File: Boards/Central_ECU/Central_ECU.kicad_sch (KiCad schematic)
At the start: 88 parts, among them J1 Micro_SD_Card, U1 SSD1306, U2 STM32G0B1RCTx, U3 TCAN1046, U9 LPS22HH, Y1 8MHz, Y2 32.768k

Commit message: Updates to board to refelct rework state
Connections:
- net CAN1_RX: now also TP10.1, TP11.1, TP8.1, U2.25 (PC4), U2.26 (PC5), U3.4 (RXD1), U3.6 (TXD2), U3.7 (RXD2); no longer U2.27 (PB0)
- net CAN2_RX: now also U2.27 (PB0); no longer TP10.1, U2.25 (PC4), U3.6 (TXD2)
- net CAN2_TX: now also U2.28 (PB1); no longer TP11.1, U2.26 (PC5), U3.7 (RXD2)
- removed net CAN1_TX: TP8.1, U2.28 (PB1), U3.4 (RXD1)
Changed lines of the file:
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@@
 	(wire
 		(pts
+			(xy 100.33 105.41) (xy 100.33 113.03)
+		)
+		(stroke
+			(width 0)
+			(type default)
+		)
+	)
+	(wire
+		(pts
 			(xy 129.54 91.44) (xy 129.54 105.41)
 		)
@@
 	(wire
 		(pts
+			(xy 109.22 109.22) (xy 109.22 115.57)
+		)
+		(stroke
+			(width 0)
+			(type default)
+		)
+	)
+	(wire
+		(pts
 			(xy 323.85 102.87) (xy 323.85 118.11)
 		)
@@
 	(wire
 		(pts
+			(xy 106.68 109.22) (xy 109.22 109.22)
+		)
+		(stroke
+			(width 0)
+			(type default)
+		)
+	)
+	(wire
+		(pts
 			(xy 180.34 67.31) (xy 162.56 67.31)
 		)
@@
 	(wire
 		(pts
+			(xy 106.68 102.87) (xy 106.68 109.22)
+		)
+		(stroke
+			(width 0)
+			(type default)
+		)
+	)
+	(wire
+		(pts
 			(xy 246.38 177.8) (xy 246.38 172.72)
 		)
@@
 		)
 	)
-	(label "CAN2_TX"
+	(label "CAN1_TX"
 		(at 177.8 115.57 180)
 		(effects
@@
 		)
 	)
-	(label "CAN2_RX"
+	(label "CAN1_RX"
 		(at 177.8 113.03 180)
 		(effects
@@
 		)
 	)
-	(label "CAN1_TX"
+	(label "CAN2_TX"
 		(at 248.92 107.95 180)
 		(effects
@@
 		)
 	)
-	(label "CAN1_RX"
+	(label "CAN2_RX"
 		(at 248.92 105.41 180)
 		(effects

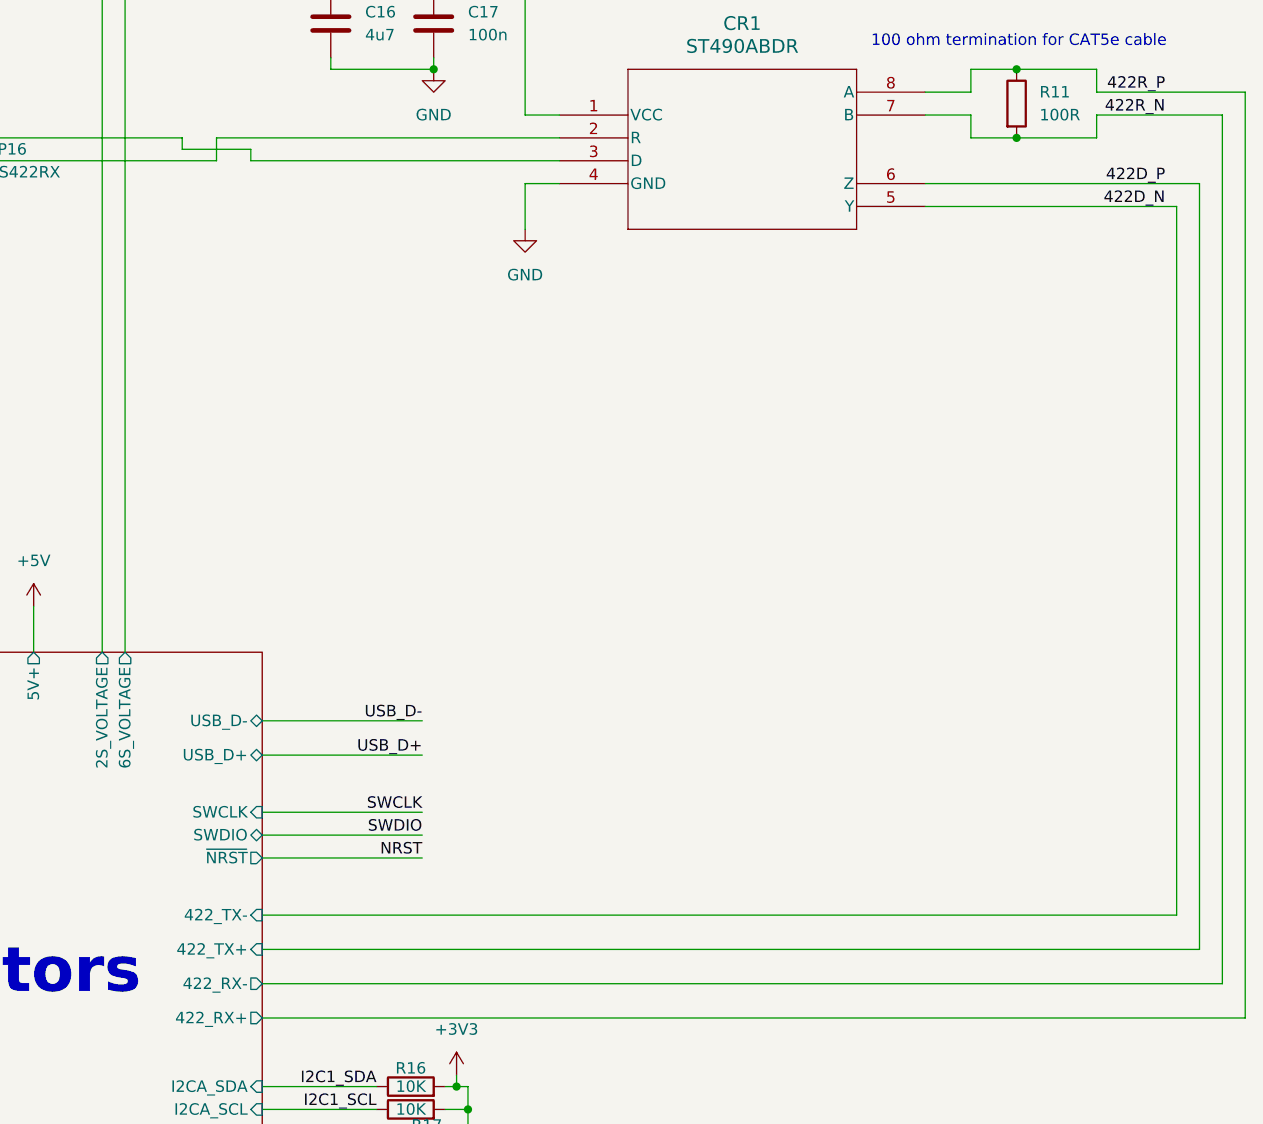
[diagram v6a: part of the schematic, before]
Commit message: Changes to reflect incorrect schematic labeling
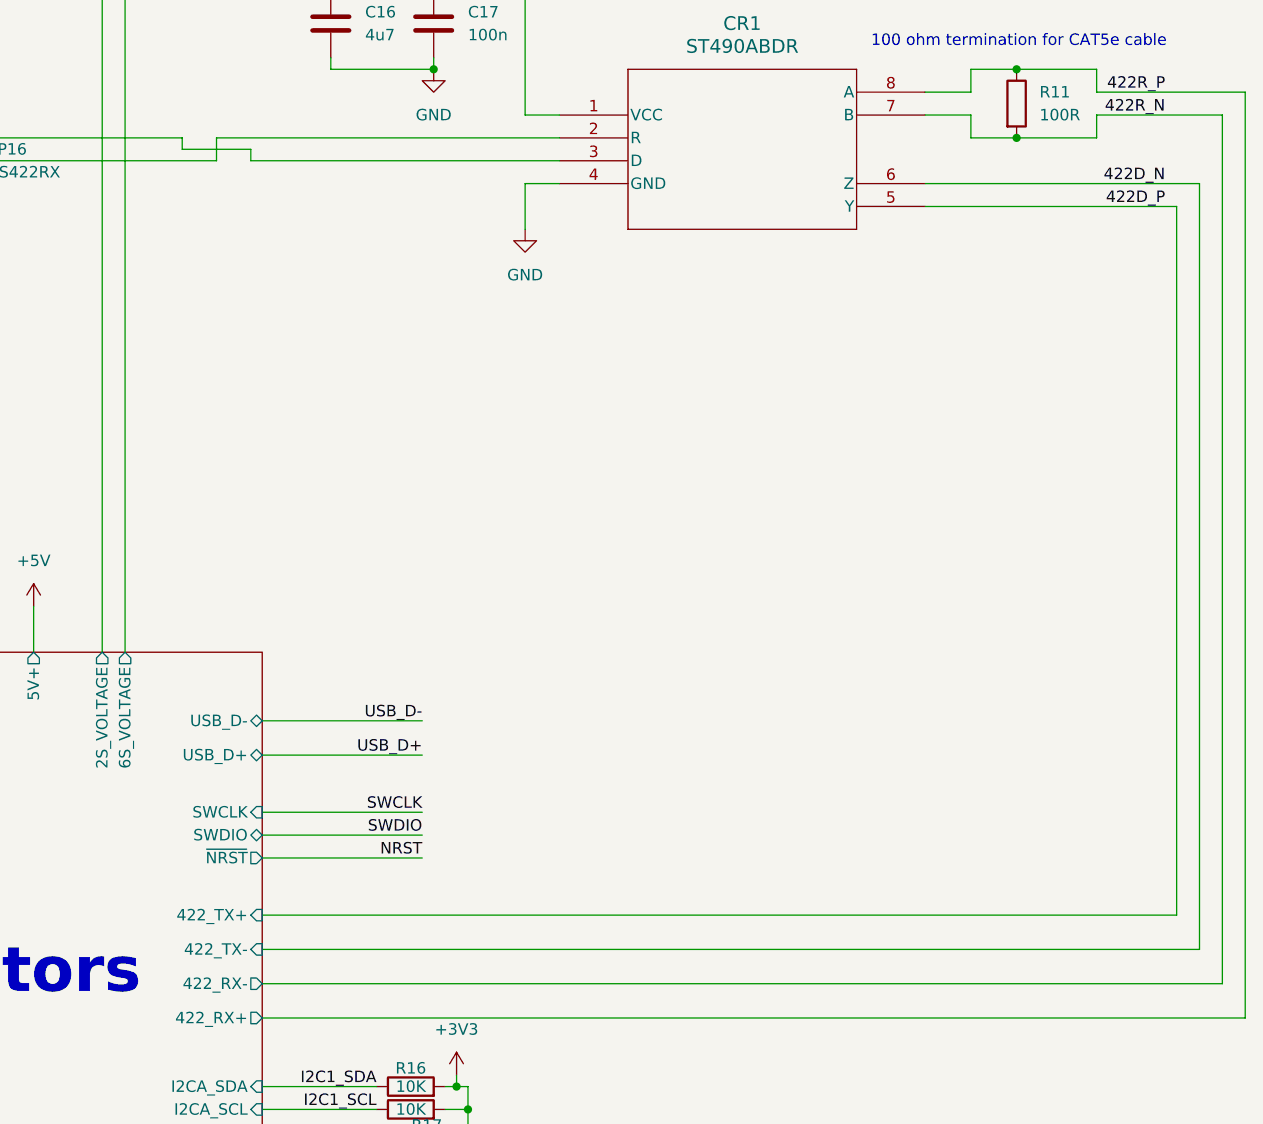
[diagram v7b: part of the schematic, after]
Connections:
- net 422D_N: now also CR1.6 (Z); no longer CR1.5 (Y)
- net 422D_P: now also CR1.5 (Y); no longer CR1.6 (Z)
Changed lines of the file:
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@@
 		)
 	)
-	(label "422D_N"
+	(label "422D_P"
 		(at 394.97 128.27 180)
 		(effects
@@
 		)
 	)
-	(label "422D_P"
+	(label "422D_N"
 		(at 394.97 125.73 180)
 		(effects
@@
 			)
 		)
-		(pin "422_TX+" input
+		(pin "422_TX-" input
 			(at 294.64 210.82 0)
 			(effects
@@
 			)
 		)
-		(pin "422_TX-" input
+		(pin "422_TX+" input
 			(at 294.64 207.01 0)
 			(effects
